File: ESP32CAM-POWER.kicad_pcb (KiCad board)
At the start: 2 copper layers, 33.5 x 39 mm, 18 parts, among them J1 Conn_01x02_Female, J2 Conn_01x06_Male, U1 D-SUN-MP1584EN, U2 ESP32-CAM

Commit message: some chages for V1.3
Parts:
- added C1: 100nF, Capacitor_SMD:C_0603_1608Metric, F.Cu at (154.5, 64.1)
- added D3: BZV55C5V1, Diode_SMD:D_MiniMELF, F.Cu at (168.8, 89.4)
- added D5: WS2812B, LED_SMD:LED_WS2812B_PLCC4_5.0x5.0mm_P3.2mm, B.Cu at (127.8, 102.6)
- added D6: WS2812B, LED_SMD:LED_WS2812B_PLCC4_5.0x5.0mm_P3.2mm, B.Cu at (172.0, 102.6)
- added D7: WS2812B, LED_SMD:LED_WS2812B_PLCC4_5.0x5.0mm_P3.2mm, B.Cu at (172.0, 57.1)
- added D8: WS2812B, LED_SMD:LED_WS2812B_PLCC4_5.0x5.0mm_P3.2mm, B.Cu at (127.8, 57.1)
- added J3: Conn_01x02_Male, Jumper:SolderJumper-2_P1.3mm_Open_RoundedPad1.0x1.5mm, F.Cu at (174.1, 92.3)
- added R3: 10k, Resistor_SMD:R_0603_1608Metric, F.Cu at (154.5, 65.6)
- added SW1: BOOT, Button_Switch_SMD:SW_Push_1P1T_NO_6x6mm_H9.5mm, F.Cu at (156.1, 58.2)
- added kibuzzard-61893861: G***, kibuzzard-61893861, F.Cu at (180.3, 80.2)
- added kibuzzard-61893876: G***, kibuzzard-61893876, F.Cu at (141.9, 51.4)
- added kibuzzard-61893880: G***, kibuzzard-61893880, F.Cu at (147.0, 51.4)
- added kibuzzard-61893893: G***, kibuzzard-61893893, F.Cu at (144.4, 51.4)
- added kibuzzard-6189389B: G***, kibuzzard-6189389B, F.Cu at (136.8, 51.4)
- added kibuzzard-61893A2D: G***, kibuzzard-61893A2D, F.Cu at (156.8, 85.1)
- added kibuzzard-61893D50: G***, kibuzzard-61893D50, F.Cu at (128.3, 84.1)
- added kibuzzard-61893E19: G***, kibuzzard-61893E19, F.Cu at (156.1, 52.2)
- added kibuzzard-619E5A56: G***, kibuzzard-619E5A56, F.Cu at (148.8, 81.1)
- added kibuzzard-619E5D40: G***, kibuzzard-619E5D40, F.Cu at (128.3, 62.1)
- U1: moved to B.Cu
- moved H4 141.4 mm to (186.0, 80.0)
- moved D4 114.6 mm to (158.6, 93.0), turned to 0 degrees
- moved U1 111.0 mm to (168.8, 79.9), turned to -90 degrees
- moved kibuzzard-611BC01E 102.6 mm to (168.8, 84.3)
- moved kibuzzard-611BC02E 101.6 mm to (175.2, 62.5)
- moved kibuzzard-611BC015 100.8 mm to (168.8, 69.6)
- moved D2 98.5 mm to (168.8, 85.7)
- moved D1 96.3 mm to (168.7, 72.7)
- moved R2 95.9 mm to (168.8, 87.4), turned to 0 degrees
- moved kibuzzard-611BBF3F 94.2 mm to (171.4, 65.0)
- moved R1 93.2 mm to (168.7, 71.1)
- moved kibuzzard-611BBF47 91.8 mm to (171.7, 59.9)
- moved H1 84.8 mm to (150.0, 116.0)
- moved J1 84.7 mm to (164.4, 59.9), turned to -90 degrees
- moved U2 82.4 mm to (140.0, 80.0)
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- renumbered D2 to D1, D3 to D2, D1 to D4
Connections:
- D4 pad 2: Net-(D1-Pad2) (its old number) -> Net-(J2-Pad3)
- J2 pad 1: Net-(D1-Pad2) (its old number) -> GND
- J2 pad 2: TX -> unconnected-(J2-Pad2)
- J2 pad 3: RX -> Net-(J2-Pad3)
- J2 pad 4: GND -> RX
- J2 pad 5: GND -> TX
- J2 pad 6: BOOT -> unconnected-(J2-Pad6)
- U1 pad 7: +5V -> Net-(U1-Pad7)
- U1 pad 8: +5V -> Net-(U1-Pad7)
- U2 pad 10: (no net) -> unconnected-(U2-Pad10)
- U2 pad 13: (no net) -> unconnected-(U2-Pad13)
- U2 pad 3: (no net) -> LED
- U2 pad 4: (no net) -> unconnected-(U2-Pad4)
- U2 pad 5: (no net) -> unconnected-(U2-Pad5)
- U2 pad 6: (no net) -> unconnected-(U2-Pad6)
- U2 pad 7: (no net) -> unconnected-(U2-Pad7)
- U2 pad 8: (no net) -> unconnected-(U2-Pad8)
- U2 pad 9: (no net) -> +3V3
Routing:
- net +5V: track 45.8 -> 181.6 mm, vias 0 -> 1
- net Net-(D5-Pad2): track 0.00 -> 53.4 mm
- net Net-(D6-Pad2): track 0.00 -> 50.1 mm, vias 0 -> 2
- net Net-(J2-Pad3): track 0.00 -> 46.2 mm, vias 0 -> 1
- net Net-(D7-Pad2): track 0.00 -> 41.7 mm
- net LED: track 0.00 -> 36.6 mm, vias 0 -> 1
- net VCC: track 49.2 -> 22.5 mm
- net BOOT: track 3.71 -> 16.3 mm
- net TX: track 3.71 -> 13.3 mm
- net Net-(U1-Pad7): track 0.00 -> 5.97 mm
- net Net-(D1-Pad2) (its old number): track 4.96 -> 0.00 mm
- net GND: track 0.00 -> 3.76 mm, vias 0 -> 9
- net +3V3: track 0.00 -> 3.18 mm
- net RX: track 3.71 -> 5.27 mm
- net Net-(D1-Pad2): track 1.39 -> 2.27 mm
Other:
- board size 33.5 x 39 mm -> 80 x 80 mm
- board text removed: "2021 Bouni"
- board text removed: "ESP32-CAM Power Board V1.1"
- board text removed: "JLCJLCJLCJLC"

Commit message: serveral changes, add USB, still a bit messy
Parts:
- removed J3: Conn_01x02_Male, Jumper:SolderJumper-2_P1.3mm_Open_RoundedPad1.0x1.5mm
- removed kibuzzard-61893876: G***, kibuzzard-61893876
- removed kibuzzard-61893880: G***, kibuzzard-61893880
- removed kibuzzard-61893893: G***, kibuzzard-61893893
- removed kibuzzard-6189389B: G***, kibuzzard-6189389B
- removed kibuzzard-61893E19: G***, kibuzzard-61893E19
- added C2: 1uF, Capacitor_SMD:C_0603_1608Metric, F.Cu at (164.7, 63.4)
- added C3: 20pF, Capacitor_SMD:C_0603_1608Metric, F.Cu at (160.8, 52.8)
- added C4: 20pF, Capacitor_SMD:C_0603_1608Metric, F.Cu at (154.8, 52.8)
- added D10: 1N4148WS, Diode_SMD:D_SOD-323, F.Cu at (160.1, 64.0)
- added D9: 1N4148WS, Diode_SMD:D_SOD-323, F.Cu at (162.2, 64.0)
- added SW2: BOOT, bouni:TS-1187A-B-A-B, F.Cu at (151.0, 63.5)
- added TP1: TestPoint, TestPoint:TestPoint_Pad_D1.5mm, F.Cu at (167.1, 84.8)
- added TP2: TestPoint, TestPoint:TestPoint_Pad_D1.5mm, F.Cu at (167.1, 78.7)
- added TP3: TestPoint, TestPoint:TestPoint_Pad_D1.5mm, F.Cu at (167.1, 81.8)
- added TP4: TestPoint, TestPoint:TestPoint_Pad_D1.5mm, F.Cu at (167.1, 75.7)
- added U3: ME6206A33XG, Package_TO_SOT_SMD:SOT-23, F.Cu at (168.3, 64.6)
- added U4: CH340G, Package_SO:SOIC-16_3.9x9.9mm_P1.27mm, F.Cu at (161.0, 58.4)
- added Y1: 12Mhz, Crystal:Crystal_SMD_3225-4Pin_3.2x2.5mm, F.Cu at (157.8, 52.8)
- added kibuzzard-61C9B144: G***, kibuzzard-61C9B144, F.Cu at (176.5, 80.3)
- added kibuzzard-61C9B1FB: G***, kibuzzard-61C9B1FB, F.Cu at (141.0, 59.5)
- added kibuzzard-61C9B205: G***, kibuzzard-61C9B205, F.Cu at (151.0, 59.5)
- added kibuzzard-61CABD37: G***, kibuzzard-61CABD37, F.Cu at (164.3, 81.8)
- added kibuzzard-61CABD44: G***, kibuzzard-61CABD44, F.Cu at (163.6, 75.7)
- added kibuzzard-61CABD72: G***, kibuzzard-61CABD72, F.Cu at (164.1, 84.8)
- added kibuzzard-61CABDE1: G***, kibuzzard-61CABDE1, F.Cu at (163.6, 78.7)
- C1: value 100nF -> 1uF
- D3: value BZV55C5V1 -> LED_O; footprint Diode_SMD:D_MiniMELF -> LED_SMD:LED_0603_1608Metric
- D4: value 1N4148WS -> SN4001W; footprint Diode_SMD:D_SOD-323 -> Diode_SMD:D_SOD-123
- J1: footprint Connector_Phoenix_MSTB:PhoenixContact_MSTBVA_2,5_2-G-5,08_1x02_P5.08mm_Vertical -> TerminalBlock_RND:TerminalBlock_RND_205-00232_1x02_P5.08mm_Horizontal
- J2: value Conn_01x06_Male -> USB_B_Micro; footprint Connector_PinHeader_2.54mm:PinHeader_1x06_P2.54mm_Horizontal -> Connector_USB:USB_Micro-B_Amphenol_10118194_Horizontal
- R2, R3: value 10k -> 680
- SW1: value BOOT -> RESET; footprint Button_Switch_SMD:SW_Push_1P1T_NO_6x6mm_H9.5mm -> bouni:TS-1187A-B-A-B
- moved kibuzzard-61893861 55.3 mm to (125.0, 80.5)
- moved J2 41.0 mm to (176.4, 53.6), turned to 135 degrees
- moved D4 31.6 mm to (172.8, 64.8), turned to 90 degrees
- moved R3 28.0 mm to (178.8, 79.5), turned to 0 degrees
- moved J1 21.2 mm to (183.6, 68.8), turned to 112.5 degrees
- moved kibuzzard-611BBF47 18.2 mm to (185.0, 72.3), turned to 22.5 degrees
- moved C1 16.3 mm to (170.8, 64.8), turned to 90 degrees
- moved SW1 16.1 mm to (140.8, 63.5), turned to 180 degrees
- moved D3 13.1 mm to (178.8, 81.0), turned to 0 degrees
- moved D1 10.9 mm to (178.8, 76.7)
- moved R1 10.9 mm to (178.8, 75.1), turned to 0 degrees
- moved R2 10.7 mm to (178.8, 83.7)
- moved kibuzzard-611BBF3F 10.2 mm to (180.6, 60.6), turned to 22.5 degrees
- moved D2 10.0 mm to (178.8, 85.2)
- moved kibuzzard-611BC015 9.88 mm to (176.5, 75.8), turned to 90 degrees
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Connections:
- C1 pad 1: BOOT -> VSS
- D3 pad 1: +5V -> GND
- D3 pad 2: GND -> Net-(D3-A)
- D4 pad 2: Net-(J2-Pad3) -> VSS
- J2 pad 1: GND -> VSS
- J2 pad 2: unconnected-(J2-Pad2) -> D-
- J2 pad 3: Net-(J2-Pad3) -> D+
- J2 pad 4: RX -> unconnected-(J2-ID)
- J2 pad 5: TX -> GND
- J2 pad 6: unconnected-(J2-Pad6) -> GND
- R3 pad 1: +3V3 -> VSS
- R3 pad 2: BOOT -> Net-(D3-A)
- SW1 pad 2: BOOT -> RESET
- U1 pad 2: GND -> VCC
- U1 pad 3: VCC -> GND
- U1 pad 4: VCC -> +5V
- U2 pad 16: GND -> RESET
- U2 pad 9: +3V3 -> unconnected-(U2-3V3)
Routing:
- net +5V: track 181.6 -> 21.7 mm
- net Net-(J2-Pad3): track 46.2 -> 0.00 mm, vias 1 -> 0
- net VSS: track 0.00 -> 38.9 mm
- net RESET: track 0.00 -> 32.3 mm, vias 0 -> 2
- net RX: track 5.27 -> 36.1 mm, vias 0 -> 2
- net TX: track 13.3 -> 36.7 mm, vias 0 -> 2
- net +3V3: track 3.18 -> 25.1 mm, vias 0 -> 2
- net D-: track 0.00 -> 21.1 mm
- net D+: track 0.00 -> 18.7 mm
- net BOOT: track 16.3 -> 28.7 mm, vias 0 -> 2
- net Net-(D5-DOUT): track 53.4 -> 45.3 mm
- net GND: track 3.76 -> 11.7 mm, vias 9 -> 13
- net Net-(C3-Pad1): track 0.00 -> 6.39 mm
- net Net-(U1-Pad7): track 5.97 -> 0.00 mm
- net LED: track 36.6 -> 30.8 mm
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- added copper zone on B.Cu, net +5V

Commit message: minor cleanups
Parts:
- removed D4: SN4001W, Diode_SMD:D_SOD-123
- removed kibuzzard-61893A2D: G***, kibuzzard-61893A2D
- removed kibuzzard-619E5A56: G***, kibuzzard-619E5A56
- added D11: SN4001W, Diode_SMD:D_SOD-123, F.Cu at (172.8, 64.8)
- added TP5: TestPoint, TestPoint:TestPoint_Pad_D1.5mm, F.Cu at (166.8, 99.6)
- added kibuzzard-611BC015: G***, kibuzzard-611BC015, F.Cu at (166.8, 97.2)
- D3: value LED_O -> LED_B
- moved kibuzzard-611BC015 28.9 mm to (166.8, 103.0)
- moved D3 28.8 mm to (154.0, 95.5)
- moved R3 28.8 mm to (154.0, 94.0), turned to 180 degrees
- moved kibuzzard-61C9B144 28.2 mm to (154.0, 97.2), turned to 0 degrees
- moved kibuzzard-61CABD44 27.3 mm to (163.6, 103.0), turned to 90 degrees
- moved kibuzzard-61CABDE1 26.1 mm to (154.0, 103.0), turned to 90 degrees
- moved TP2 24.6 mm to (154.0, 99.6)
- moved TP4 24.2 mm to (163.6, 99.6)
- moved D1 22.4 mm to (166.8, 95.6), turned to 180 degrees
- moved R1 22.4 mm to (166.8, 94.0)
- moved kibuzzard-61CABD37 21.6 mm to (160.4, 103.0), turned to 90 degrees
- moved D2 21.1 mm to (160.4, 95.5), turned to 180 degrees
- moved R2 21.1 mm to (160.4, 94.0)
- moved kibuzzard-611BC01E 20.6 mm to (160.4, 97.2), turned to 0 degrees
- moved kibuzzard-61CABD72 19.4 mm to (157.2, 103.0), turned to 90 degrees
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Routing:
- net VCC: track 16.8 -> 45.6 mm
- net +3V3: track 25.1 -> 50.5 mm
- net VSS: track 38.9 -> 59.9 mm, vias 0 -> 2
- net +5V: track 21.7 -> 10.2 mm, vias 1 -> 2
- net Net-(D3-A): track 1.54 -> 2.24 mm
- net Net-(D2-A): track 1.54 -> 2.24 mm
- net Net-(D1-A): track 1.60 -> 2.27 mm
- net GND: vias 13 -> 12

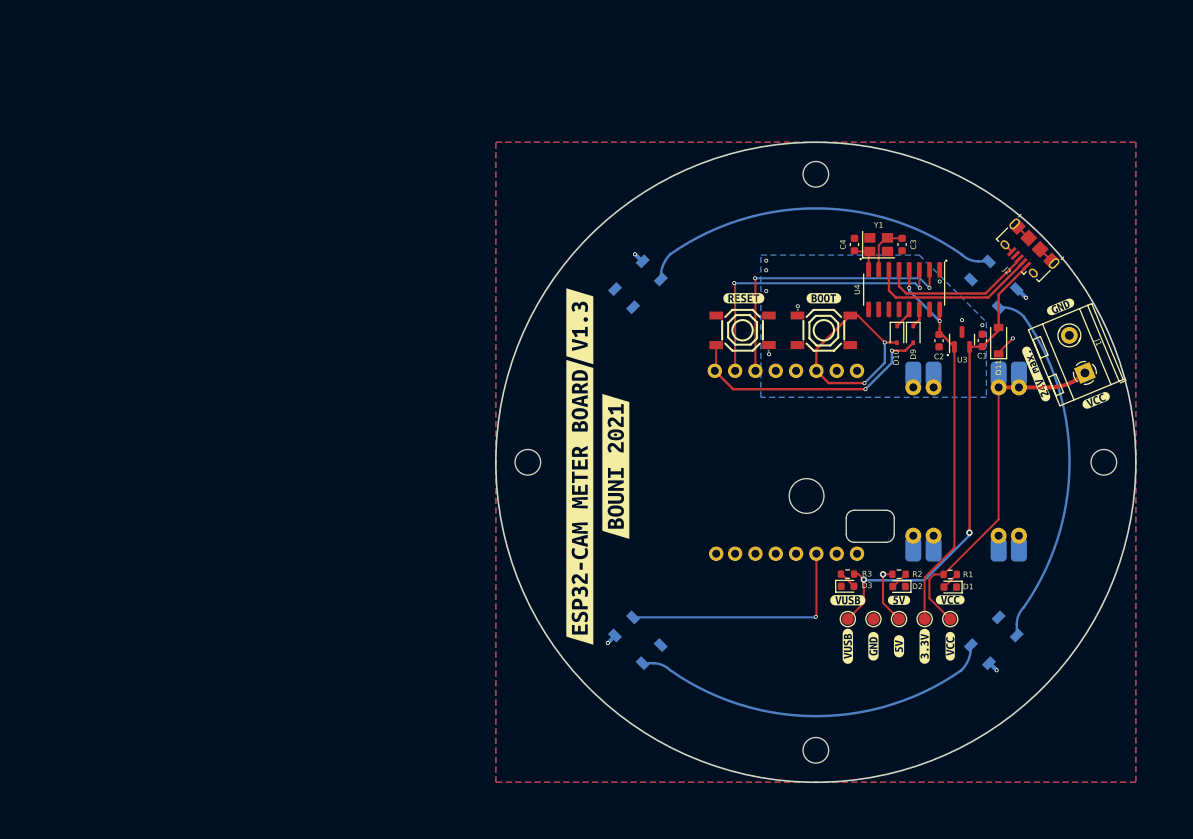
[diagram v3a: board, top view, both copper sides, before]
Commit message: massiv rework, mostly simplified the project
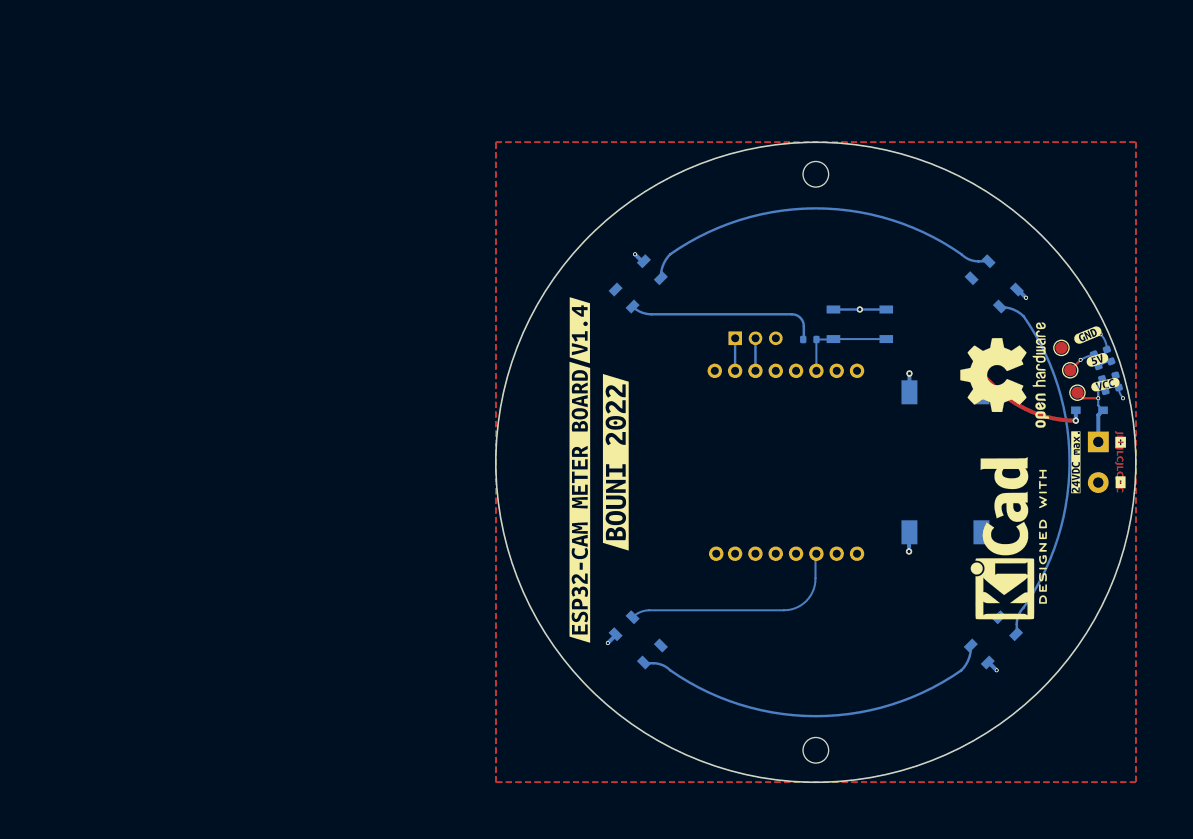
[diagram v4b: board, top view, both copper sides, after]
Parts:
- removed C1, C2: 1uF, Capacitor_SMD:C_0603_1608Metric
- removed C3, C4: 20pF, Capacitor_SMD:C_0603_1608Metric
- removed D10, D9: 1N4148WS, Diode_SMD:D_SOD-323
- removed D11: SN4001W, Diode_SMD:D_SOD-123
- removed D5, D6, D7, D8: WS2812B, LED_SMD:LED_WS2812B_PLCC4_5.0x5.0mm_P3.2mm
- removed H3, H4: MountingHole, MountingHole:MountingHole_3.2mm_M3_ISO14580
- removed SW2: BOOT, bouni:TS-1187A-B-A-B
- removed TP4, TP5: TestPoint, TestPoint:TestPoint_Pad_D1.5mm
- removed U3: ME6206A33XG, Package_TO_SOT_SMD:SOT-23
- removed U4: CH340G, Package_SO:SOIC-16_3.9x9.9mm_P1.27mm
- removed Y1: 12Mhz, Crystal:Crystal_SMD_3225-4Pin_3.2x2.5mm
- removed kibuzzard-611BBF3F: G***, kibuzzard-611BBF3F
- removed kibuzzard-611BBF47: G***, kibuzzard-611BBF47
- removed the kibuzzard-611BC015 at (166.8, 97.2)
- removed kibuzzard-611BC01E: G***, kibuzzard-611BC01E
- removed kibuzzard-611BC02E: G***, kibuzzard-611BC02E
- removed kibuzzard-61893861: G***, kibuzzard-61893861
- removed kibuzzard-61893D50: G***, kibuzzard-61893D50
- removed kibuzzard-619E5D40: G***, kibuzzard-619E5D40
- removed kibuzzard-61C9B144: G***, kibuzzard-61C9B144
- removed kibuzzard-61C9B1FB: G***, kibuzzard-61C9B1FB
- removed kibuzzard-61CABD44: G***, kibuzzard-61CABD44
- removed kibuzzard-61CABDE1: G***, kibuzzard-61CABDE1
- added LED1: XL-5050RGBC-WS2812B, LCSC:LED-SMD_4P-L5.0-W5.0-BL_XL-5050RGBC, B.Cu at (127.8, 102.2)
- added LED2: XL-5050RGBC-WS2812B, LCSC:LED-SMD_4P-L5.0-W5.0-BL_XL-5050RGBC, B.Cu at (172.2, 102.2)
- added LED3: XL-5050RGBC-WS2812B, LCSC:LED-SMD_4P-L5.0-W5.0-BL_XL-5050RGBC, B.Cu at (172.3, 57.7)
- added LED4: XL-5050RGBC-WS2812B, LCSC:LED-SMD_4P-L5.0-W5.0-BL_XL-5050RGBC, B.Cu at (127.8, 57.7)
- added REF**: KiCad-Logo2_8mm_SilkScreen, Symbol:KiCad-Logo2_8mm_SilkScreen, F.Cu at (173.3, 89.5)
- added REF**: OSHW-Logo2_14.6x12mm_SilkScreen, Symbol:OSHW-Logo2_14.6x12mm_SilkScreen, F.Cu at (173.6, 69.1)
- added kibuzzard-62976962: G***, kibuzzard-62976962, F.Cu at (182.5, 80.0)
- added kibuzzard-6297697D: G***, kibuzzard-6297697D, F.Cu at (188.1, 77.5)
- added kibuzzard-629769A0: G***, kibuzzard-629769A0, F.Cu at (188.1, 82.5)
- added kibuzzard-62976FF9: G***, kibuzzard-62976FF9, B.Cu at (145.0, 60.6)
- added kibuzzard-62977004: G***, kibuzzard-62977004, B.Cu at (142.4, 60.6)
- added kibuzzard-62977011: G***, kibuzzard-62977011, B.Cu at (139.9, 60.6)
- added kibuzzard-62989351: G***, kibuzzard-62989351, F.Cu at (125.0, 80.0)
- added kibuzzard-6298938A: G***, kibuzzard-6298938A, F.Cu at (120.5, 85.0)
- added kibuzzard-629893A5: G***, kibuzzard-629893A5, F.Cu at (120.5, 63.5)
- D1: value LED_R -> LED_Y; moved to B.Cu
- D2, R1, R2, kibuzzard-61C9B205: moved to B.Cu
- D3: value LED_B -> D_Schottky; footprint LED_SMD:LED_0603_1608Metric -> LCSC:SOD-123_L2.7-W1.6-LS3.7-RD-1; moved to B.Cu
- J1: value Conn_01x02_Female -> Screw_Terminal_01x02; footprint TerminalBlock_RND:TerminalBlock_RND_205-00232_1x02_P5.08mm_Horizontal -> TerminalBlock_Phoenix:TerminalBlock_Phoenix_MKDS-1,5-2-5.08_1x02_P5.08mm_Horizontal; moved to B.Cu
- J2: value USB_B_Micro -> Conn_01x03_Male; footprint Connector_USB:USB_Micro-B_Amphenol_10118194_Horizontal -> Connector_PinHeader_2.54mm:PinHeader_1x03_P2.54mm_Vertical; moved to B.Cu
- R3: value 680 -> 10k; moved to B.Cu
- SW1: value RESET -> TS-1187A-B-A-B; footprint bouni:TS-1187A-B-A-B -> LCSC:SW-SMD_4P-L5.1-W5.1-P3.70-LS6.5-TL-2; moved to B.Cu
- U1: value D-SUN-MP1584EN -> DC-DC-BOARD; footprint bouni:D-SUN-MP1584EN -> bouni:DC-DC-MODULE
- moved kibuzzard-61CABD72 47.2 mm to (184.0, 64.1), turned to 22.5 degrees
- moved kibuzzard-61CABD37 43.6 mm to (185.2, 67.2), turned to 17.5 degrees
- moved TP2 41.7 mm to (181.8, 68.5)
- moved TP1 41.2 mm to (180.7, 65.7)
- moved D2 39.0 mm to (186.7, 66.7), turned to -70 degrees
- moved J2 38.1 mm to (139.9, 64.5), turned to -90 degrees
- moved kibuzzard-611BC015 38.0 mm to (186.2, 70.3), turned to 12.5 degrees
- moved D3 37.4 mm to (184.2, 73.5)
- moved R2 36.4 mm to (185.1, 67.2), turned to -70 degrees
- moved TP3 36.0 mm to (182.7, 71.3)
- moved D1 33.1 mm to (187.7, 69.9), turned to 105 degrees
- moved R1 30.5 mm to (186.0, 70.3), turned to -75 degrees
- moved R3 29.7 mm to (149.3, 64.7), turned to 0 degrees
- moved SW1 14.7 mm to (155.5, 62.8)
- moved J1 8.78 mm to (185.3, 77.5), turned to -90 degrees
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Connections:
- D3 pad 1: GND -> Net-(D3-K)
- D3 pad 2: Net-(D3-A) -> VCC
- J2 pad 1: VSS -> TX
- J2 pad 2: D- -> RX
- J2 pad 3: D+ -> GND
- R3 pad 1: VSS -> +5V
- R3 pad 2: Net-(D3-A) -> BOOT
- SW1 pad 2: RESET -> GND
- SW1 pad 3: unconnected-(SW1-Pad3) -> BOOT
- SW1 pad 4: unconnected-(SW1-Pad4) -> BOOT
- TP2 pad 1: VSS -> +5V
- TP3 pad 1: +5V -> VCC
- U1 pad 2: VCC -> Net-(D3-K)
- U1 pad 3: GND -> +5V
- U1 pad 4: +5V -> GND
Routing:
- net VSS: track 59.9 -> 0.00 mm, vias 2 -> 0
- net +3V3: track 50.5 -> 0.00 mm, vias 2 -> 0
- net Net-(D6-DOUT): track 45.3 -> 0.00 mm
- net Net-(LED1-DO): track 0.00 -> 45.3 mm
- net Net-(D5-DOUT): track 45.3 -> 0.00 mm
- net Net-(LED3-DO): track 0.00 -> 45.3 mm
- net Net-(D7-DOUT): track 45.3 -> 0.00 mm
- net Net-(LED2-DO): track 0.00 -> 44.9 mm
- net VCC: track 45.6 -> 11.4 mm, vias 0 -> 1
- net TX: track 36.7 -> 4.07 mm, vias 2 -> 0
- net RESET: track 32.3 -> 0.00 mm, vias 2 -> 0
- net RX: track 36.1 -> 4.07 mm, vias 2 -> 0
- net D-: track 21.1 -> 0.00 mm
- net D+: track 18.7 -> 0.00 mm
- net +5V: track 10.2 -> 27.7 mm, vias 2 -> 1
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- removed copper zone on B.Cu, net GND
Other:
- outline, holes or cut-outs redrawn
- board text added: "JLCJLCJLCJLC"
- board text removed: "D-SUN MP1584EN"

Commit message: fixed short circuit caused by mounting holes
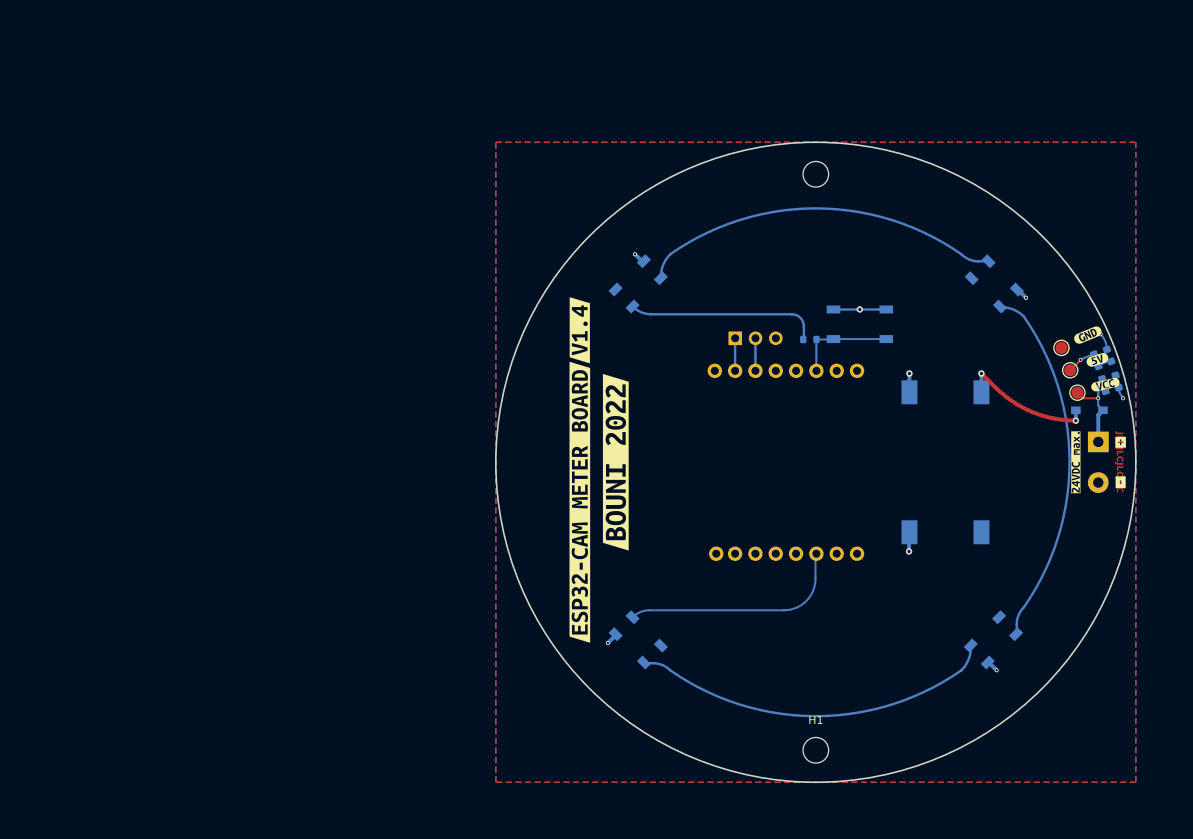
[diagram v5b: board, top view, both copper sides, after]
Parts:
- removed REF**: KiCad-Logo2_8mm_SilkScreen, Symbol:KiCad-Logo2_8mm_SilkScreen
- removed REF**: OSHW-Logo2_14.6x12mm_SilkScreen, Symbol:OSHW-Logo2_14.6x12mm_SilkScreen
